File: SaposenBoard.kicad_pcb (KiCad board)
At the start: 2 copper layers, 60 x 50 mm, 79 parts, among them IC1 BSO220, IC2 BSO220, IC3 BSO220, IC4 BSO220, J1 ADC4ch, J2 Extra2ch+LED, J3 I2C, J4 Encoder1, J5 Encoder2, J6 Motor1, J7 Motor2, J8 Battery, Q1 IRLML6344, Q2 IRLML6344, Q3 IRLML6344, Q4 IRLML6344, Q5 IRLML6344, SW1 SW_Push, SW2 SW_Push, SW3 BatterySW, U1 A4955GLPTR-T, U2 A4955GLPTR-T, U3 MPU-6500, U4 NUCLEO-F303K8

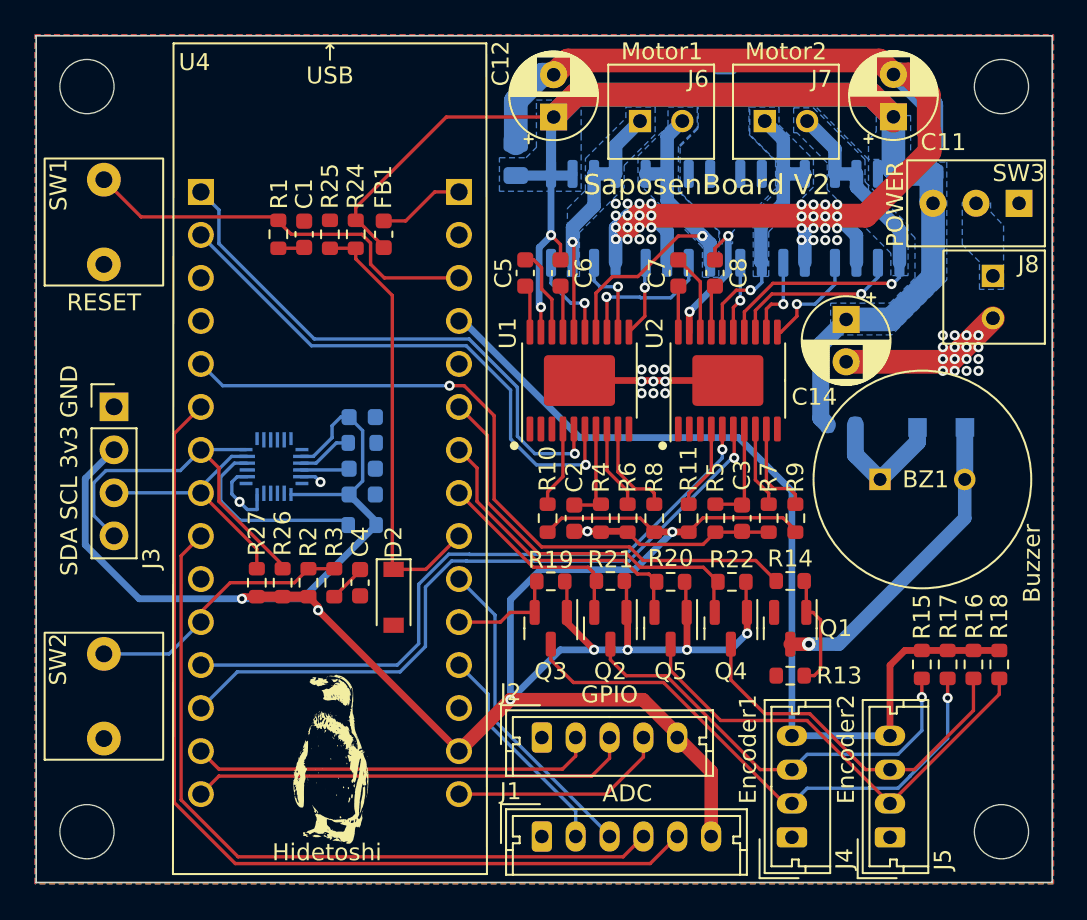
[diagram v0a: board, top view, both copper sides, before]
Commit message: [update]アンテナ除去
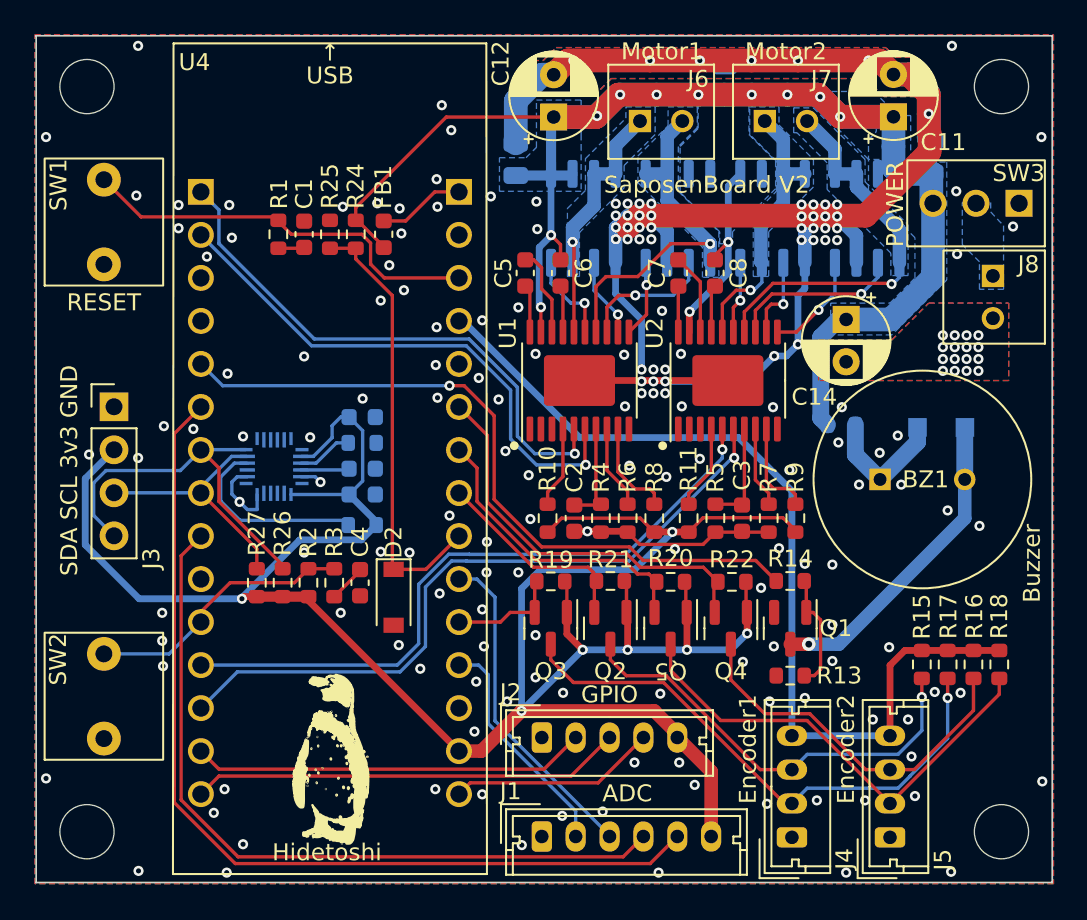
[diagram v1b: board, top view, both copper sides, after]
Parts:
- removed the REF** at (106.7, 88.9)
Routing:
- net GND: track 105.7 -> 116.9 mm, vias 60 -> 197
- net +BATT: track 111.9 -> 114.9 mm, vias 4 -> 12
- net +3V3: track 145.5 -> 144.7 mm, vias 8 -> 7
- net Extra2: track 26.2 -> 25.5 mm
- net SDA: track 22.9 -> 22.2 mm
- net ADC1: track 13.0 -> 13.7 mm
- net NUCLEO_LED: track 12.9 -> 12.3 mm
- net Extra1: track 24.0 -> 23.3 mm
- net Net-(IC1-Pad2): track 5.29 -> 4.67 mm
- net ADC2: track 18.9 -> 19.5 mm

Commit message: [update]IMU位置見直し
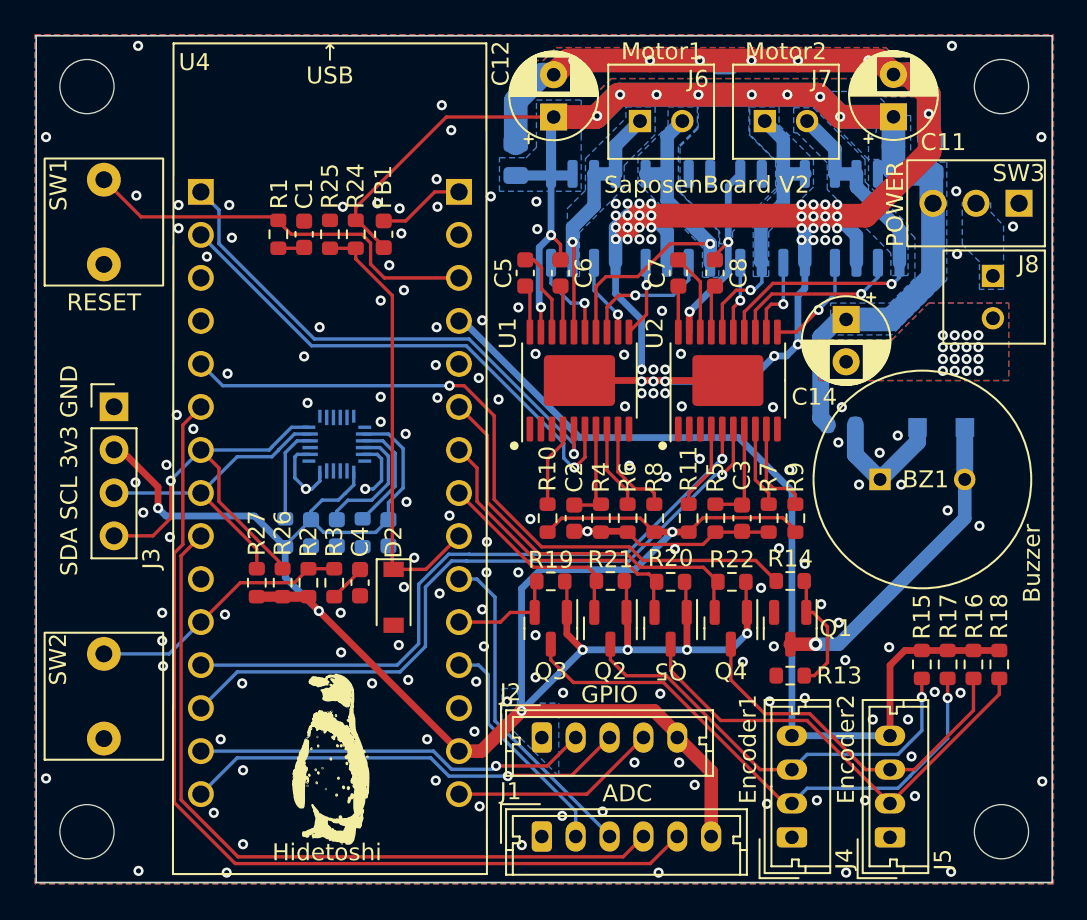
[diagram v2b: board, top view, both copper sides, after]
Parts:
- moved C15 7.01 mm to (120.8, 79.3), turned to -90 degrees
- moved R23 5.31 mm to (119.3, 79.3), turned to 90 degrees
- moved R28 4.57 mm to (114.7, 79.3), turned to 90 degrees
- moved C16 4.07 mm to (117.8, 79.3), turned to -90 degrees
- moved U3 3.94 mm to (117.8, 74.1)
- moved C17 3.77 mm to (116.2, 79.3), turned to -90 degrees
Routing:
- net +3V3: track 144.7 -> 138.9 mm, vias 7 -> 8
- net Net-(R28-Pad2): track 11.4 -> 5.66 mm
- net Net-(C16-Pad1): track 2.88 -> 7.51 mm
- net SCLK: track 14.8 -> 18.9 mm
- net Net-(R23-Pad2): track 3.30 -> 6.84 mm
- net GND: track 116.9 -> 119.4 mm, vias 197 -> 205
- net SDA: track 22.2 -> 24.3 mm, vias 0 -> 1
- net MOT1_IN2: track 32.8 -> 31.4 mm
- net MOT1_IN1: track 32.2 -> 30.8 mm
- net Extra2: track 25.5 -> 26.4 mm, vias 0 -> 1
- net Extra1: track 23.3 -> 23.4 mm, vias 0 -> 1

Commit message: [fix]部品を変更
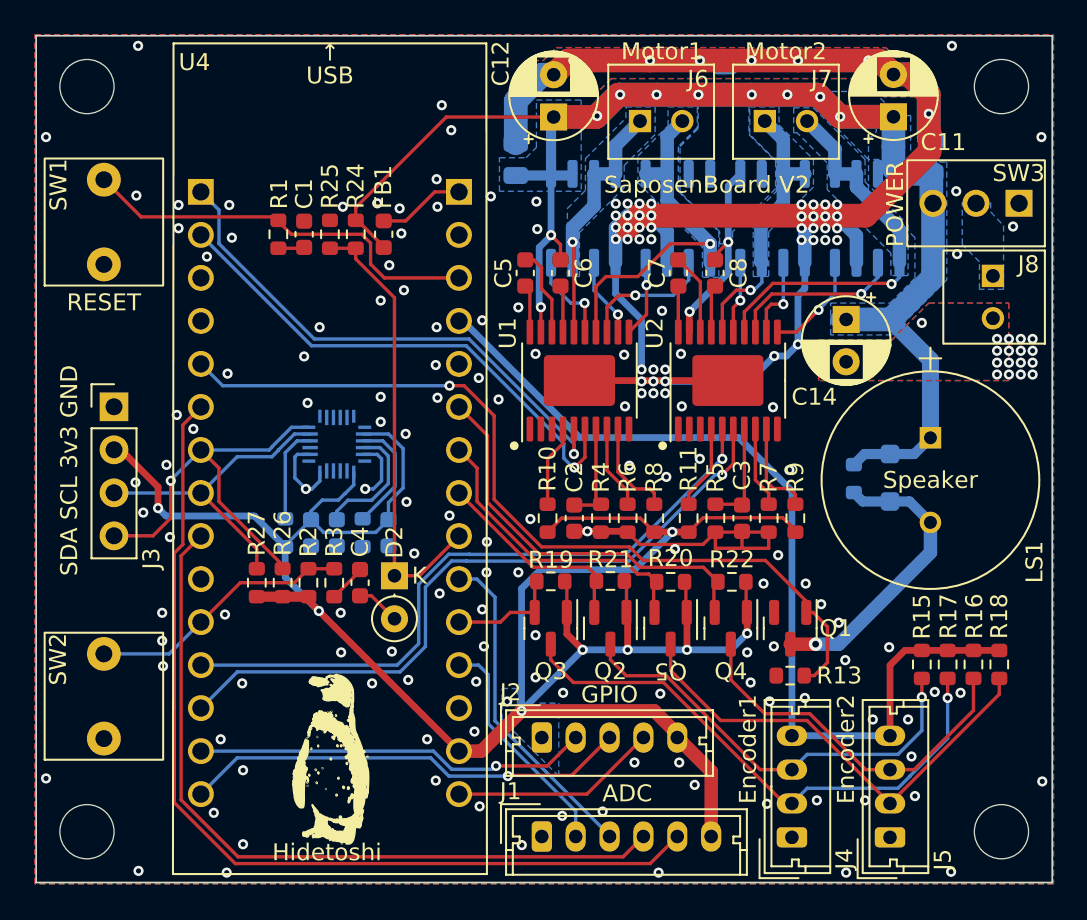
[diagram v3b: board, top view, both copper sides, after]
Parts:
- removed BZ1: Buzzer, Footprints:PKM13EPYH4000-A0
- removed R14: 30, Resistor_SMD:R_0603_1608Metric
- added LS1: Speaker, Footprints:PKM13EPYH4000-A0, F.Cu at (152.8, 73.7)
- D2: value MMSZ4684-TP -> 1N5226B; footprint Diode_SMD:D_SOD-123 -> Diode_THT:D_DO-35_SOD27_P2.54mm_Vertical_KathodeUp
- G***: footprint My:penpen -> Footprints:penpen
- Q1, Q2, Q3, Q4, Q5: value IRLML6344 -> BSS138
- moved D1 4.24 mm to (150.4, 76.1), turned to -90 degrees
- moved R12 3.26 mm to (148.3, 76.1), turned to 90 degrees
- moved D2 1.27 mm to (121.2, 81.9)
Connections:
- D1 pad 1: Net-(BZ1-Pad1) -> +BATT
- D1 pad 2: Net-(BZ1-Pad2) -> Net-(D1-A)
- Q1 pad 1: Net-(Q1-Pad1) -> SPEAKER
- Q1 pad 3: Net-(BZ1-Pad2) -> Net-(D1-A)
- R12 pad 1: Net-(BZ1-Pad1) -> Net-(D1-A)
- R13 pad 2: Net-(Q1-Pad1) -> SPEAKER
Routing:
- net Net-(BZ1-Pad2): track 18.8 -> 0.00 mm, vias 1 -> 0
- net Net-(D1-A): track 0.00 -> 17.6 mm, vias 0 -> 1
- net GND: track 119.4 -> 128.1 mm, vias 205 -> 199
- net SPEAKER: track 42.2 -> 50.5 mm
- net Net-(BZ1-Pad1): track 7.82 -> 0.00 mm
- net Net-(Q1-Pad1): track 7.31 -> 0.00 mm
- net +BATT: track 114.9 -> 121.0 mm
- net Net-(D2-K): track 26.1 -> 26.6 mm
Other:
- board text added: "Remove R12 to use Fan."

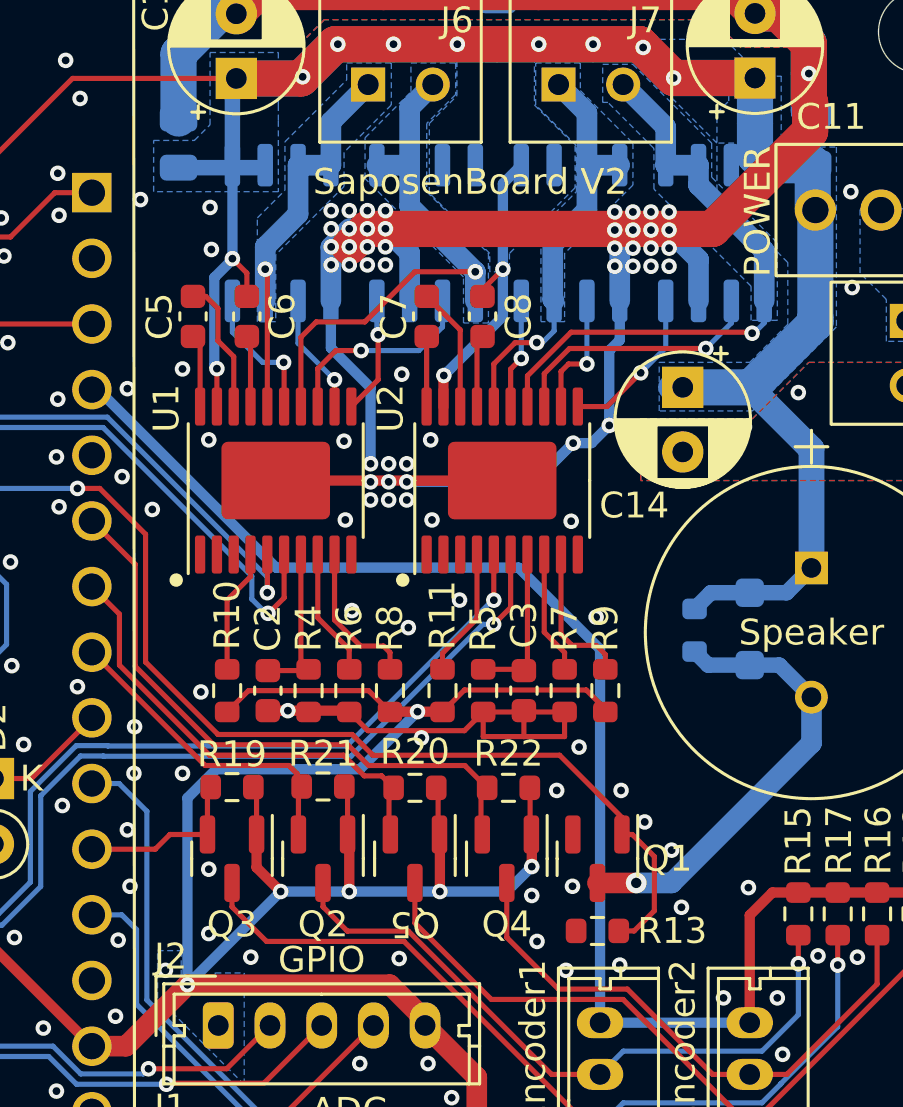
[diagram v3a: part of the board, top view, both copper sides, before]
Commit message: [add]ロゴ変更
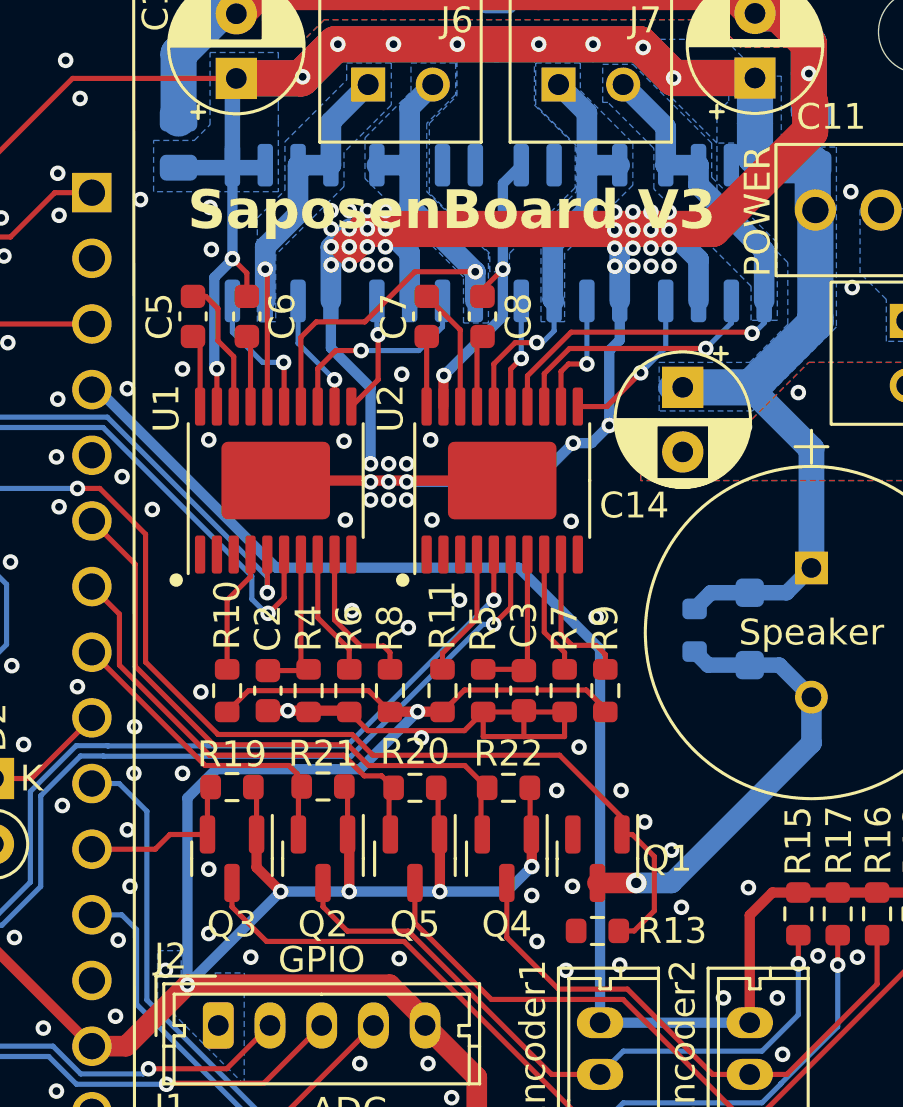
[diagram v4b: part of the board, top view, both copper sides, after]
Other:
- board text added: "Exclude D1 for piezo."
- board text added: "SaposenBoard V3"
- board text removed: "Remove R12 to use Fan."
- board text removed: "SaposenBoard V2"

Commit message: [update]部品置いた
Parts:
- removed the C1 at (115.8, 61.7)
- removed the C13 at (152.9, 57.1)
- removed C3: 470p, Capacitor_SMD:C_0603_1608Metric
- removed R5: 47k, Resistor_SMD:R_0603_1608Metric
- removed SW1: SW_Push, Footprints:TVDT18-050C
- added C15: 10u, Capacitor_SMD:C_0805_2012Metric, B.Cu at (152.9, 57.1)
- added C2: 470p, Capacitor_SMD:C_0603_1608Metric, F.Cu at (140.2, 78.2)
- added J4: ADC_Extend, Connector_Molex:Molex_Micro-Latch_53253-0470_1x04_P2.00mm_Vertical, F.Cu at (135.6, 95.8)
- added Q1: BSS138, Package_TO_SOT_SMD:SOT-23, B.Cu at (129.8, 77.0)
- added Q2: BSS138, Package_TO_SOT_SMD:SOT-23, B.Cu at (143.0, 78.5)
- added R15: 470, Resistor_SMD:R_0603_1608Metric, F.Cu at (116.8, 83.8)
- added R18: 10k, Resistor_SMD:R_0603_1608Metric, B.Cu at (112.8, 94.0)
- added R2: 10k, Resistor_SMD:R_0603_1608Metric, B.Cu at (143.0, 75.9)
- added R4: 10k, Resistor_SMD:R_0603_1608Metric, B.Cu at (137.4, 77.0)
- added R9: 33k, Resistor_SMD:R_0603_1608Metric, F.Cu at (143.3, 78.2)
- added U1: 74CBTLV3257, Package_SO:TSSOP-16_4.4x5mm_P0.65mm, B.Cu at (117.6, 95.2)
- added U2: ~, Package_TO_SOT_SMD:SOT-363_SC-70-6, B.Cu at (133.1, 77.0)
- added U3: ~, Package_TO_SOT_SMD:SOT-363_SC-70-6, B.Cu at (139.7, 77.0)
- J1: value ADC4ch -> ADC
- J2: value Extra2ch+LED -> ADC/Servo; footprint Connector_Molex:Molex_Micro-Latch_53253-0570_1x05_P2.00mm_Vertical -> Connector_PinHeader_2.54mm:PinHeader_2x03_P2.54mm_Vertical
- R1, R3: value 470 -> 10k; moved to B.Cu
- R17: renamed from R13; value 47k -> 10k
- R28: renamed from R24; value 1.8k -> 33k
- R29: renamed from R25; value 1k -> 10k
- R30: renamed from R26; value 4.7k -> 1k
- R31: renamed from R27; value 4.7k -> 1k
- R32: renamed from R28; value 4.7k -> 10k
- R7: value 33k -> 47k
- SW2: value SW_Push -> SW
- moved J2 42.8 mm to (102.5, 58.5)
- moved R1 23.4 mm to (129.5, 79.5), turned to 0 degrees
- moved R3 18.6 mm to (135.4, 77.0), turned to 90 degrees
- moved D2 17.3 mm to (118.9, 64.8), turned to 180 degrees
- moved J1 11.6 mm to (139.7, 91.2), turned to 180 degrees
- moved R30 2.75 mm to (112.3, 83.8)
- moved J3 2.51 mm to (103.5, 74.2)
- moved C4 1.70 mm to (118.4, 83.8)
- moved R10 1.70 mm to (115.3, 83.8), turned to -90 degrees
- moved R31 1.70 mm to (113.8, 83.8)
- moved R7 1.55 mm to (141.7, 78.2)
- moved C13 0.41 mm to (120.4, 79.3)
- moved C14 0.41 mm to (117.3, 79.3)
- moved C17 0.41 mm to (115.8, 79.3)
- moved R27 0.41 mm to (118.9, 79.3)
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- renumbered C2 to C1, C15 to C13, C16 to C14, C14 to C16, J4 to J5, J5 to J6, J6 to J7, J7 to J8, J8 to J9, Q1 to Q3, Q2 to Q4, Q3 to Q5, Q4 to Q6, Q5 to Q7, R2 to R10, R8 to R11, R9 to R12, R10 to R13, R11 to R14, R12 to R16, R15 to R19, R16 to R20, R17 to R21, R18 to R22, R19 to R23, R20 to R24, R21 to R25, R22 to R26, R23 to R27, R4 to R6, R6 to R8, U1 to U4, U2 to U5, U4 to U6, U3 to U7
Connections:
- net SCLK renamed /SCLK
- net SDA renamed /SDA
- net SPEAKER renamed /SPEAKER
- J1 pad 2: ADC1 -> /Sensor1_4
- J1 pad 3: ADC2 -> /Sensor1_3
- J1 pad 4: ADC3 -> /Sensor1_2
- J1 pad 5: ADC4 -> /Sensor1_1
- J2 pad 1: GND -> /ADC2_2
- J2 pad 2: Extra1 -> /ADC2_1
- J2 pad 3: Extra2 -> +3V3
- J2 pad 4: NUCLEO_LED -> +3V3
- J2 pad 5: +3V3 -> GND
- Q4 pad 2: ENC1_2 -> /ENC1_1
- Q5 pad 2: ENC1_1 -> /ENC1_2
- Q6 pad 2: ENC2_2 -> /ENC2_1
- Q7 pad 2: ENC2_1 -> /ENC2_2
- R1 pad 1: NRST -> /MOT1_EN
- R1 pad 2: Net-(C1-Pad1) -> GND
- R10 pad 2: SW1 -> /SW1
- R23 pad 1: ENC1_1 -> /ENC1_2
- R24 pad 1: ENC2_1 -> /ENC2_2
- R25 pad 1: ENC1_2 -> /ENC1_1
- R26 pad 1: ENC2_2 -> /ENC2_1
- R3 pad 1: SW1 -> Net-(Q1-D)
- R3 pad 2: Net-(C4-Pad1) -> +3V3
- R7 pad 1: Net-(U2-ISET) -> Net-(U5-RC)
- SW2 pad 2: SW1 -> /SW1
- U4 pad 5: MOT1_IN2 -> Net-(U2-Y0)
- U4 pad 6: MOT1_IN1 -> Net-(U2-Y1)
- U5 pad 5: MOT2_IN2 -> Net-(U3-Y0)
- U5 pad 6: MOT2_IN1 -> Net-(U3-Y1)
- U5 pad 7: Net-(U2-RC) -> Net-(U5-RC)
- U5 pad 8: Net-(U2-ISET) -> Net-(U5-ISET)
- U6 pad 3_1: MOT1_IN2 -> /ENC2_1
- U6 pad 3_11: SW1 -> /ADC_SEL
- U6 pad 3_12: MOT2_IN2 -> /ENC2_2
- U6 pad 3_13: MOT2_IN1 -> /MOT1_PH
- U6 pad 3_14: Extra1 -> /ENC1_1
- U6 pad 3_15: Extra2 -> /ENC1_2
- U6 pad 3_2: MOT1_IN1 -> /MOT2_EN
- U6 pad 3_6: ADC4 -> /ADC3
- U6 pad 3_9: ADC3 -> /ADC4
- U6 pad 4_10: ADC2 -> /ADC2
- U6 pad 4_11: ENC1_1 -> /ADC1
- U6 pad 4_12: ADC1 -> /MOT1_EN
- U6 pad 4_15: NUCLEO_LED -> /SW1
- U6 pad 4_3: NRST -> unconnected-(U6-NRST-Pad4_3)
- U6 pad 4_6: ENC2_2 -> /ADC2_1
- U6 pad 4_7: ENC2_1 -> /ADC2_2
- U6 pad 4_8: ENC1_2 -> /MOT2_PH
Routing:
- net ADC4: track 55.9 -> 0.00 mm
- net /ENC2_1: track 0.00 -> 51.4 mm
- net ADC3: track 45.3 -> 0.00 mm
- net /MOT2_EN: track 0.00 -> 44.5 mm
- net MOT2_IN1: track 41.5 -> 0.00 mm, vias 1 -> 0
- net MOT2_IN2: track 39.7 -> 0.00 mm, vias 1 -> 0
- net /MOT1_PH: track 0.00 -> 32.7 mm, vias 0 -> 1
- net /ADC2_2: track 0.00 -> 32.5 mm
- net /ENC2_2: track 0.00 -> 32.2 mm
- net /ADC3: track 0.00 -> 32.1 mm, vias 0 -> 1
- net MOT1_IN2: track 31.4 -> 0.00 mm, vias 1 -> 0
- net /ENC1_1: track 0.00 -> 31.2 mm
- net MOT1_IN1: track 30.8 -> 0.00 mm, vias 1 -> 0
- net /ENC1_2: track 0.00 -> 29.2 mm
- net +3V3: track 138.9 -> 167.7 mm, vias 8 -> 7
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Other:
- board text removed: "SDA SCL 3v3 GND"
